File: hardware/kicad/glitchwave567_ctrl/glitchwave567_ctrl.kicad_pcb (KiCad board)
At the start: 4 copper layers, 138 x 114 mm, 22 parts, among them J1 to MAIN 2x8, SW1 Suntsu SSWFS-S01 (TAP/BYP), SW2 Suntsu SSWFS-S01 (TAP/BYP)

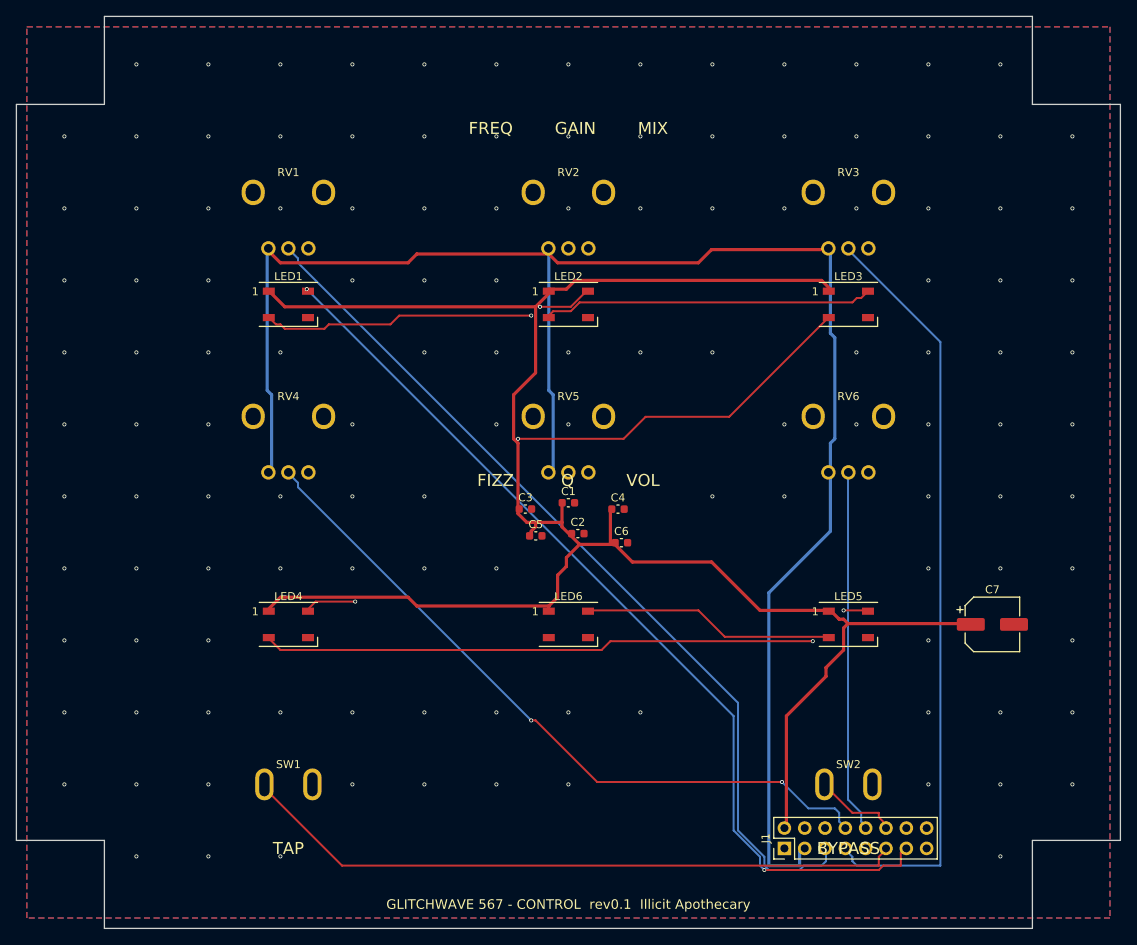
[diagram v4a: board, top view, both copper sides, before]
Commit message: Step 3: both boards fab-ready - 0 unconnected, 0 electrical DRC violations
- Main board fully routed (210/210 nets) via new exact-geometry microrouter
- Surgical DRC repair: 30+ offender vias/tracks removed and rerouted exactly
- Placement fixes: FB100 off J5 pin, C122 off U18 tab, C48/C109/R51/R69/
  R137/C50/C101-103/C97/R41 courtyard moves, all nets rejoined
- GND finalize: 54 exact-checked via-in-pad + stitching + per-fragment vias
- Dangling stub cleanup to fixpoint
- Fab package: 4-layer gerbers + drill + pos for both boards, 3D renders,
  1:1 enclosure drill template PDF, PCBWay turnkey README
- Residual: cosmetic silk overlaps, 4 shallow courtyard kisses (documented)

Co-Authored-By: Claude Fable 5 <noreply@anthropic.com>
Claude-Session: https://claude.ai/code/session_016gPfgma2WpZSHWdz1n3cWG
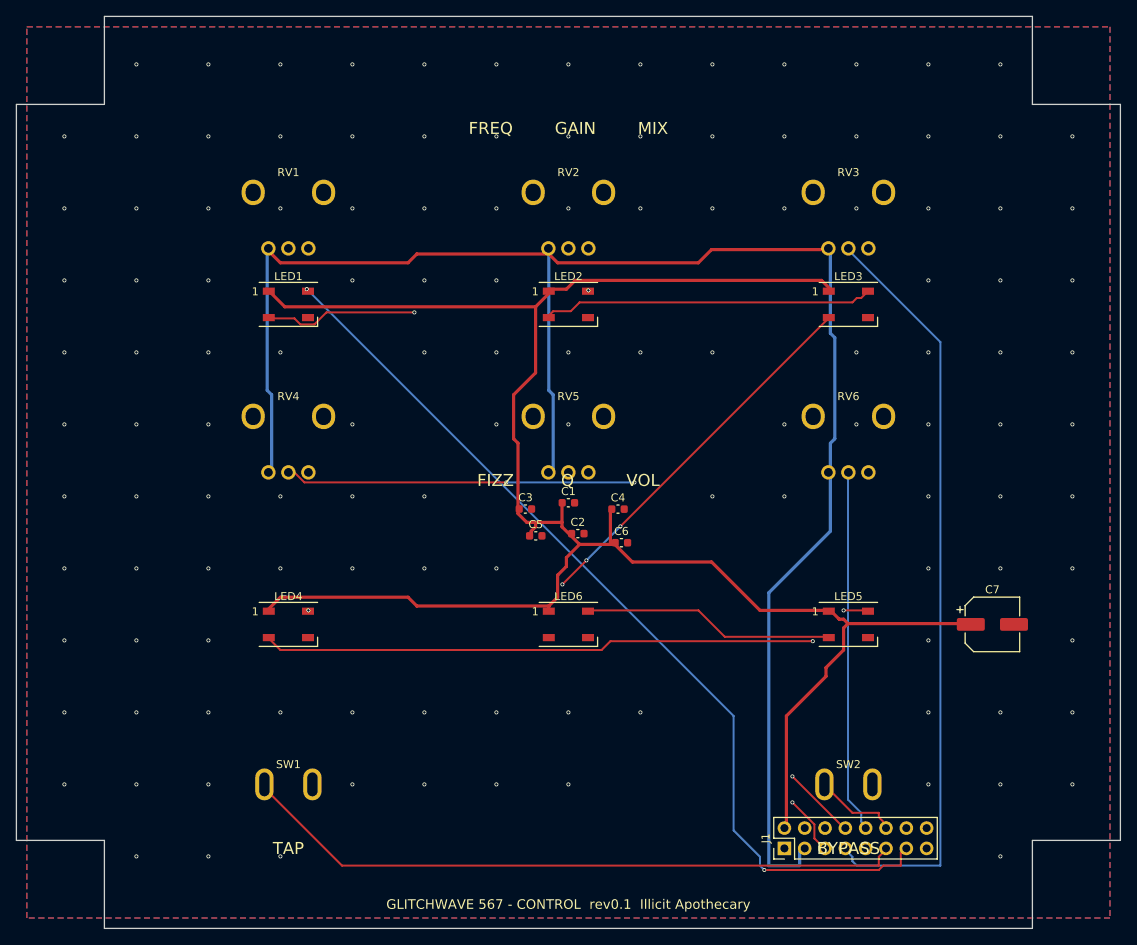
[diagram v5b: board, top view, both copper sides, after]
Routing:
- net /POT4_W: track 88.5 -> 98.0 mm, vias 2 -> 3
- net /POT1_W: track 111.6 -> 108.0 mm, vias 0 -> 1
- net /WSD1: track 42.9 -> 42.3 mm
- net /WSD3: track 80.7 -> 80.3 mm, vias 2 -> 4
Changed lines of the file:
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@@
   (segment (start 100.65 33) (end 69.85 33) (width 0.4) (layer "F.Cu") (net 1))
   (segment (start 92.95 74.25) (end 101.75 74.25) (width 0.4) (layer "F.Cu") (net 1))
-  (segment (start 98.45 106.15) (end 100.65 106.15) (width 0.25) (layer "B.Cu") (net 2))
-  (segment (start 35.2 30.25) (end 35.2 30.8) (width 0.25) (layer "B.Cu") (net 2))
-  (segment (start 93.5 106.15) (end 94.05 106.7) (width 0.25) (layer "B.Cu") (net 2))
-  (segment (start 90.2 101.75) (end 93.5 105.05) (width 0.25) (layer "B.Cu") (net 2))
-  (segment (start 35.2 30.8) (end 90.2 85.8) (width 0.25) (layer "B.Cu") (net 2))
-  (segment (start 100.65 106.15) (end 101.2 105.6) (width 0.25) (layer "B.Cu") (net 2))
-  (segment (start 101.2 105.6) (end 101.2 103.95) (width 0.25) (layer "B.Cu") (net 2))
-  (segment (start 34.1 29.15) (end 35.2 30.25) (width 0.25) (layer "B.Cu") (net 2))
-  (segment (start 94.05 106.7) (end 97.9 106.7) (width 0.25) (layer "B.Cu") (net 2))
-  (segment (start 90.2 85.8) (end 90.2 101.75) (width 0.25) (layer "B.Cu") (net 2))
-  (segment (start 93.5 105.05) (end 93.5 106.15) (width 0.25) (layer "B.Cu") (net 2))
-  (segment (start 97.9 106.7) (end 98.45 106.15) (width 0.25) (layer "B.Cu") (net 2))
+  (segment (start 101 104) (end 99.75 102.75) (width 0.25) (layer "F.Cu") (net 2))
+  (segment (start 99.75 101) (end 97 98.25) (width 0.25) (layer "F.Cu") (net 2))
+  (segment (start 101.08 104) (end 101 104) (width 0.25) (layer "F.Cu") (net 2))
+  (segment (start 99.75 102.75) (end 99.75 101) (width 0.25) (layer "F.Cu") (net 2))
+  (via (at 97 98.25) (size 0.5) (drill 0.3) (layers "F.Cu" "B.Cu") (net 2))
+  (segment (start 64 52) (end 42.25 30.25) (width 0.25) (layer "In2.Cu") (net 2))
+  (segment (start 36 30.25) (end 34.75 29) (width 0.25) (layer "In2.Cu") (net 2))
+  (segment (start 70.25 58) (end 70.25 56.5) (width 0.25) (layer "In2.Cu") (net 2))
+  (segment (start 74.75 76) (end 74.75 63) (width 0.25) (layer "In2.Cu") (net 2))
+  (segment (start 71.5 59.25) (end 70.25 58) (width 0.25) (layer "In2.Cu") (net 2))
+  (segment (start 74.75 63) (end 71.5 59.75) (width 0.25) (layer "In2.Cu") (net 2))
+  (segment (start 70.25 56.5) (end 65.75 52) (width 0.25) (layer "In2.Cu") (net 2))
+  (segment (start 97 98.25) (end 74.75 76) (width 0.25) (layer "In2.Cu") (net 2))
+  (segment (start 42.25 30.25) (end 36 30.25) (width 0.25) (layer "In2.Cu") (net 2))
+  (segment (start 71.5 59.75) (end 71.5 59.25) (width 0.25) (layer "In2.Cu") (net 2))
+  (segment (start 34.75 29) (end 34 29) (width 0.25) (layer "In2.Cu") (net 2))
+  (segment (start 65.75 52) (end 64 52) (width 0.25) (layer "In2.Cu") (net 2))
   (segment (start 99.55 99.55) (end 99 99) (width 0.25) (layer "In2.Cu") (net 3))
   (segment (start 86.35 68.2) (end 75.9 57.75) (width 0.25) (layer "In2.Cu") (net 3))
@@
   (segment (start 105.05 106.15) (end 104.5 105.6) (width 0.25) (layer "B.Cu") (net 4))
   (segment (start 115.5 106.15) (end 105.05 106.15) (width 0.25) (layer "B.Cu") (net 4))
-  (segment (start 64.9 88) (end 72.6 95.7) (width 0.25) (layer "F.Cu") (net 5))
-  (segment (start 72.6 95.7) (end 95.7 95.7) (width 0.25) (layer "F.Cu") (net 5))
-  (segment (start 64.35 88) (end 64.9 88) (width 0.25) (layer "F.Cu") (net 5))
-  (via (at 64.35 88) (size 0.5) (drill 0.3) (layers "F.Cu" "B.Cu") (net 5))
-  (via (at 95.7 95.7) (size 0.5) (drill 0.3) (layers "F.Cu" "B.Cu") (net 5))
-  (segment (start 35.2 58.85) (end 64.35 88) (width 0.25) (layer "B.Cu") (net 5))
-  (segment (start 102.85 99.55) (end 102.85 100.65) (width 0.25) (layer "B.Cu") (net 5))
-  (segment (start 95.7 95.7) (end 99 99) (width 0.25) (layer "B.Cu") (net 5))
-  (segment (start 102.85 100.65) (end 103.4 101.2) (width 0.25) (layer "B.Cu") (net 5))
-  (segment (start 102.3 99) (end 102.85 99.55) (width 0.25) (layer "B.Cu") (net 5))
-  (segment (start 99 99) (end 102.3 99) (width 0.25) (layer "B.Cu") (net 5))
-  (segment (start 34.1 57.2) (end 35.2 58.3) (width 0.25) (layer "B.Cu") (net 5))
-  (segment (start 35.2 58.3) (end 35.2 58.85) (width 0.25) (layer "B.Cu") (net 5))
+  (segment (start 61.25 58.25) (end 36 58.25) (width 0.25) (layer "F.Cu") (net 5))
+  (segment (start 34.75 57) (end 34 57) (width 0.25) (layer "F.Cu") (net 5))
+  (segment (start 103.62 101.46) (end 103.5 101.5) (width 0.25) (layer "F.Cu") (net 5))
+  (segment (start 103.5 101.5) (end 97 95) (width 0.25) (layer "F.Cu") (net 5))
+  (segment (start 36 58.25) (end 34.75 57) (width 0.25) (layer "F.Cu") (net 5))
+  (via (at 97 95) (size 0.5) (drill 0.3) (layers "F.Cu" "B.Cu") (net 5))
+  (via (at 77.25 58.25) (size 0.5) (drill 0.3) (layers "F.Cu" "B.Cu") (net 5))
+  (via (at 61.25 58.25) (size 0.5) (drill 0.3) (layers "F.Cu" "B.Cu") (net 5))
+  (segment (start 97 95) (end 86.75 84.75) (width 0.25) (layer "In2.Cu") (net 5))
+  (segment (start 86.75 84.75) (end 86.75 68) (width 0.25) (layer "In2.Cu") (net 5))
+  (segment (start 77.25 58.5) (end 77.25 58.25) (width 0.25) (layer "In2.Cu") (net 5))
+  (segment (start 86.75 68) (end 77.25 58.5) (width 0.25) (layer "In2.Cu") (net 5))
+  (segment (start 77.25 58.25) (end 61.25 58.25) (width 0.25) (layer "B.Cu") (net 5))
   (segment (start 106.15 105.6) (end 105.6 106.15) (width 0.25) (layer "In2.Cu") (net 6))
   (segment (start 94.05 106.15) (end 74.25 86.35) (width 0.25) (layer "In2.Cu") (net 6))
@@
   (segment (start 107.8 100.1) (end 108.9 101.2) (width 0.25) (layer "F.Cu") (net 9))
   (segment (start 101.2 96.25) (end 104.5 99.55) (width 0.25) (layer "F.Cu") (net 9))
-  (segment (start 32.45 38.5) (end 31.35 37.4) (width 0.25) (layer "F.Cu") (net 10))
-  (segment (start 64.35 37.4) (end 47.85 37.4) (width 0.25) (layer "F.Cu") (net 10))
-  (segment (start 69.3 36.3) (end 65.45 36.3) (width 0.25) (layer "F.Cu") (net 10))
-  (segment (start 33.55 39.05) (end 33 38.5) (width 0.25) (layer "F.Cu") (net 10))
-  (segment (start 39.05 38.5) (end 38.5 39.05) (width 0.25) (layer "F.Cu") (net 10))
-  (segment (start 33 38.5) (end 32.45 38.5) (width 0.25) (layer "F.Cu") (net 10))
-  (segment (start 71.5 34.1) (end 69.3 36.3) (width 0.25) (layer "F.Cu") (net 10))
-  (segment (start 47.85 37.4) (end 46.75 38.5) (width 0.25) (layer "F.Cu") (net 10))
-  (segment (start 38.5 39.05) (end 33.55 39.05) (width 0.25) (layer "F.Cu") (net 10))
-  (segment (start 46.75 38.5) (end 39.05 38.5) (width 0.25) (layer "F.Cu") (net 10))
-  (via (at 64.35 37.4) (size 0.5) (drill 0.3) (layers "F.Cu" "B.Cu") (net 10))
-  (via (at 65.45 36.3) (size 0.5) (drill 0.3) (layers "F.Cu" "B.Cu") (net 10))
-  (segment (start 65.45 36.3) (end 64.35 37.4) (width 0.25) (layer "In2.Cu") (net 10))
+  (segment (start 71.5 34.25) (end 71.45 34.35) (width 0.25) (layer "F.Cu") (net 10))
+  (segment (start 38.75 37) (end 49.75 37) (width 0.25) (layer "F.Cu") (net 10))
+  (segment (start 37.25 38.5) (end 38.75 37) (width 0.25) (layer "F.Cu") (net 10))
+  (segment (start 34.75 37.75) (end 35.5 38.5) (width 0.25) (layer "F.Cu") (net 10))
+  (segment (start 31.55 37.65) (end 31.5 37.75) (width 0.25) (layer "F.Cu") (net 10))
+  (segment (start 31.5 37.75) (end 34.75 37.75) (width 0.25) (layer "F.Cu") (net 10))
+  (segment (start 35.5 38.5) (end 37.25 38.5) (width 0.25) (layer "F.Cu") (net 10))
+  (via (at 49.75 37) (size 0.5) (drill 0.3) (layers "F.Cu" "B.Cu") (net 10))
+  (via (at 71.5 34.25) (size 0.5) (drill 0.3) (layers "F.Cu" "B.Cu") (net 10))
+  (segment (start 52.5 34.25) (end 71.5 34.25) (width 0.25) (layer "In2.Cu") (net 10))
+  (segment (start 49.75 37) (end 52.5 34.25) (width 0.25) (layer "In2.Cu") (net 10))
   (segment (start 105.6 35.2) (end 106.7 34.1) (width 0.25) (layer "F.Cu") (net 11))
   (segment (start 105.05 35.2) (end 105.6 35.2) (width 0.25) (layer "F.Cu") (net 11))
@@
   (segment (start 69.3 36.85) (end 70.4 35.75) (width 0.25) (layer "F.Cu") (net 11))
   (segment (start 70.4 35.75) (end 104.5 35.75) (width 0.25) (layer "F.Cu") (net 11))
-  (segment (start 36.3 74.25) (end 37.4 73.15) (width 0.25) (layer "F.Cu") (net 12))
-  (segment (start 75.9 52.8) (end 78.65 50.05) (width 0.25) (layer "F.Cu") (net 12))
-  (segment (start 89.1 50.05) (end 101.75 37.4) (width 0.25) (layer "F.Cu") (net 12))
-  (segment (start 62.7 52.8) (end 75.9 52.8) (width 0.25) (layer "F.Cu") (net 12))
-  (segment (start 37.4 73.15) (end 42.35 73.15) (width 0.25) (layer "F.Cu") (net 12))
-  (segment (start 78.65 50.05) (end 89.1 50.05) (width 0.25) (layer "F.Cu") (net 12))
-  (via (at 62.7 52.8) (size 0.5) (drill 0.3) (layers "F.Cu" "B.Cu") (net 12))
-  (via (at 42.35 73.15) (size 0.5) (drill 0.3) (layers "F.Cu" "B.Cu") (net 12))
-  (segment (start 42.35 73.15) (end 62.7 52.8) (width 0.25) (layer "In2.Cu") (net 12))
+  (segment (start 71.25 68) (end 68.25 71) (width 0.25) (layer "F.Cu") (net 12))
+  (segment (start 36.5 74.25) (end 36.45 74.35) (width 0.25) (layer "F.Cu") (net 12))
+  (segment (start 101.55 37.65) (end 101.5 37.75) (width 0.25) (layer "F.Cu") (net 12))
+  (segment (start 101.5 37.75) (end 75.5 63.75) (width 0.25) (layer "F.Cu") (net 12))
+  (via (at 71.25 68) (size 0.5) (drill 0.3) (layers "F.Cu" "B.Cu") (net 12))
+  (via (at 68.25 71) (size 0.5) (drill 0.3) (layers "F.Cu" "B.Cu") (net 12))
+  (via (at 36.5 74.25) (size 0.5) (drill 0.3) (layers "F.Cu" "B.Cu") (net 12))
+  (via (at 75.5 63.75) (size 0.5) (drill 0.3) (layers "F.Cu" "B.Cu") (net 12))
+  (segment (start 68.25 71) (end 65 74.25) (width 0.25) (layer "In2.Cu") (net 12))
+  (segment (start 65 74.25) (end 36.5 74.25) (width 0.25) (layer "In2.Cu") (net 12))
+  (segment (start 75.5 63.75) (end 71.25 68) (width 0.25) (layer "B.Cu") (net 12))
   (segment (start 73.15 79.2) (end 74.25 78.1) (width 0.25) (layer "F.Cu") (net 13))
   (segment (start 103.4 74.25) (end 106.7 74.25) (width 0.25) (layer "F.Cu") (net 13))

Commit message: hardware: put ctrl J1 on B.Cu where it can actually mate, clear the J2 jack overlap
CONTROL BOARD - J1 was on F.Cu, the same side as the pots and stomps, while
main-board J10 is topside too. Two top-side headers 11 mm apart point away
from each other and cannot mate at all. fab/README_PCBWAY.md already says
this part "mounts on B.Cu"; the board disagreed with its own fab notes. The
63.36 mm2 J1/SW2 body overlap was a consequence: on the correct side J1's
body sits in the board-to-board gap and SW2's sits above the board, so there
is nothing to collide.

Flipping the stock footprint is NOT the fix. Mirroring a 2x08 maps the pad
grid onto itself but permutes the PIN NUMBERS - column c <-> column 9-c, so
1<->15, 2<->16, 3<->13, 4<->14, 5<->11, 6<->12, 7<->9, 8<->10. That silently
reverses the pinout: GND and +5V swap ends and the pot wipers land on the
wrong MCU inputs, with nothing in DRC to catch it. Measured, not assumed -
tools/fit_ctrl_j1.py scores each candidate against J10's real pad positions:

  stock footprint,    flip LEFT_RIGHT    ->  2/16 pads land correctly
  stock footprint,    flip TOP_BOTTOM    ->  8/16
  MIRRORED footprint, flip TOP_BOTTOM    -> 16/16   <== chosen

So: new Glitchwave.pretty/PinHeader_2x08_P2.54mm_Vertical_Mirrored.kicad_mod
(stock part with every pad's local x negated, generated by the new
tools/mirror_footprint.py), placed on B.Cu at the same (96, 104). Verified by
independent re-read after saving: side BACK, 16/16 pad positions match J10 by
pin number, 16/16 nets preserved. **Zero schematic change, zero net change**,
and because the pads are through-hole at unchanged coordinates the existing
routing still lands on them - nothing needed rerouting.

Control board after: body overlaps 0 (was 1 at 63.36 mm2), DRC 6 warnings /
0 errors / 0 unconnected, ERC 6 warnings / 0 errors. Same as baseline apart
from the collision being gone.

MAIN BOARD - J2 (the output jack) had the same defect J1 did, found by the
new tools/audit.py and invisibl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
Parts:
- J1: value to MAIN 2x8 -> to MAIN 2x8 (B.Cu, mirrored); footprint PinHeader_2x08_P2.54mm_Vertical -> PinHeader_2x08_P2.54mm_Vertical_Mirrored; moved to B.Cu
- turned J1 to -90 degrees
